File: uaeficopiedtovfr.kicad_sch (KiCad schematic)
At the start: 36 parts, among them J1 DTF13-12PB, J1 USB_B_Mini, J1 USB_C_Receptacle_USB2.0, J17 Conn_01x06, J4 DTF13-12PB, J5 Conn_01x05_Male, M1 Module-power_12and5V-0.2, M3 Module-knock-0.2, M3 Module-vr-discrete-0.4, M4 Module-vr-max9924-0.1, M5 Module-wbo-0.5, M6 Module:mega-mcu100/0.2, M7 Module-wbo-0.5, P1 Pad, P2 Pad, P3 Pad, P4 Pad, U4 JDY-33

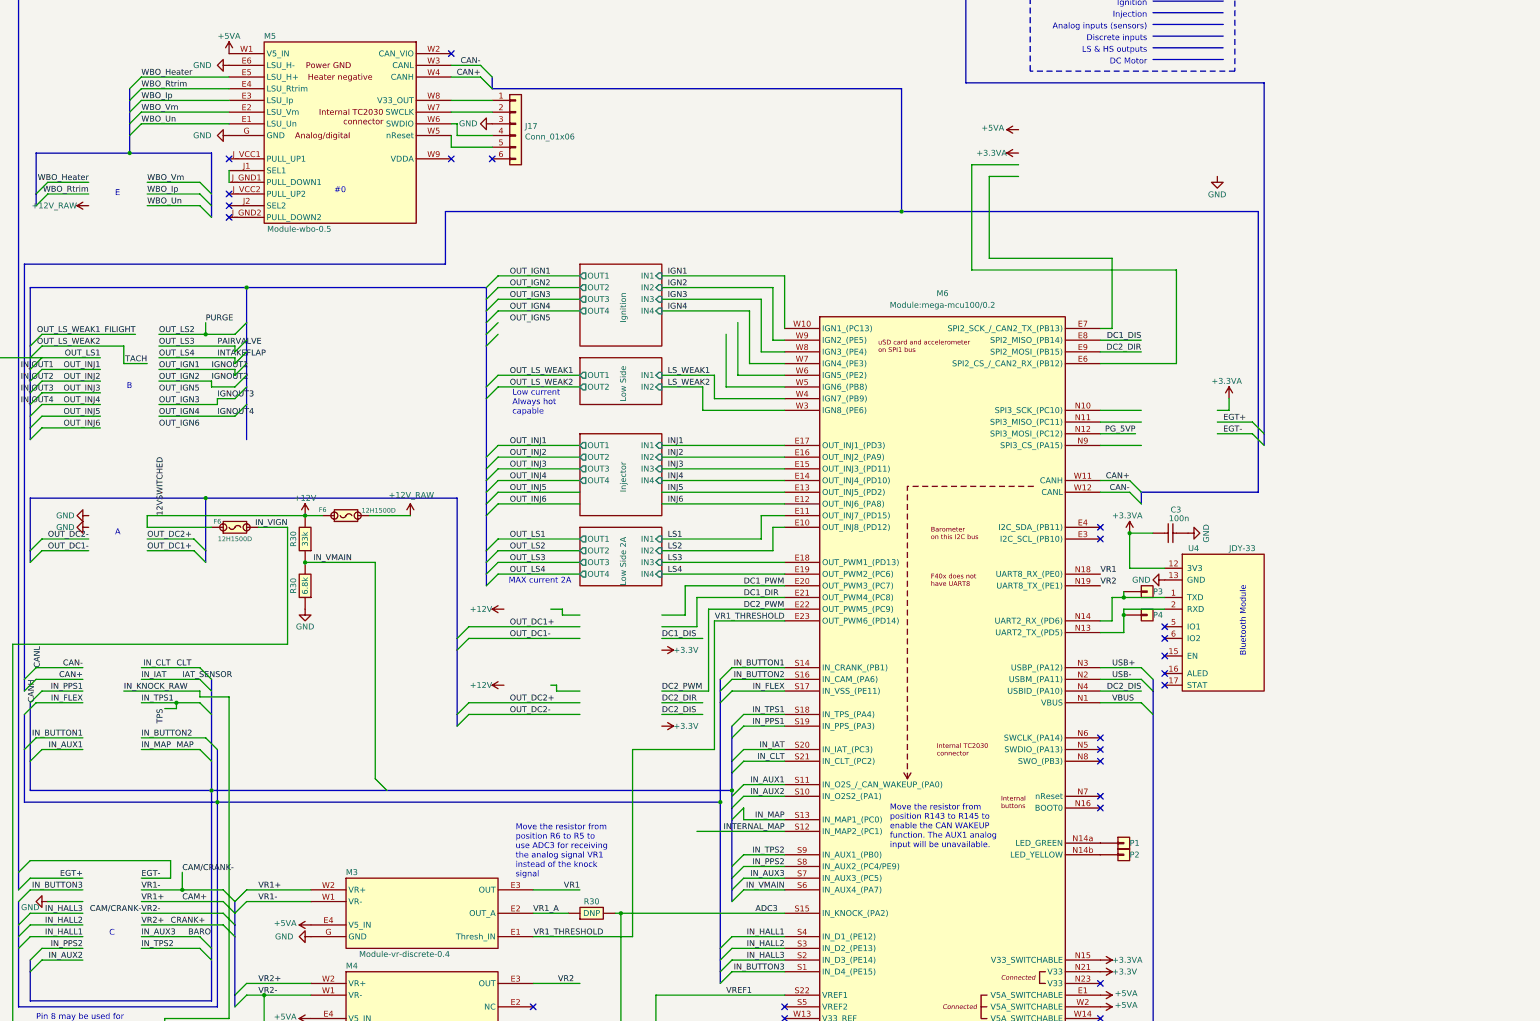
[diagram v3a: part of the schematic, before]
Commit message: Added SD card support, cleaned up ignition traces
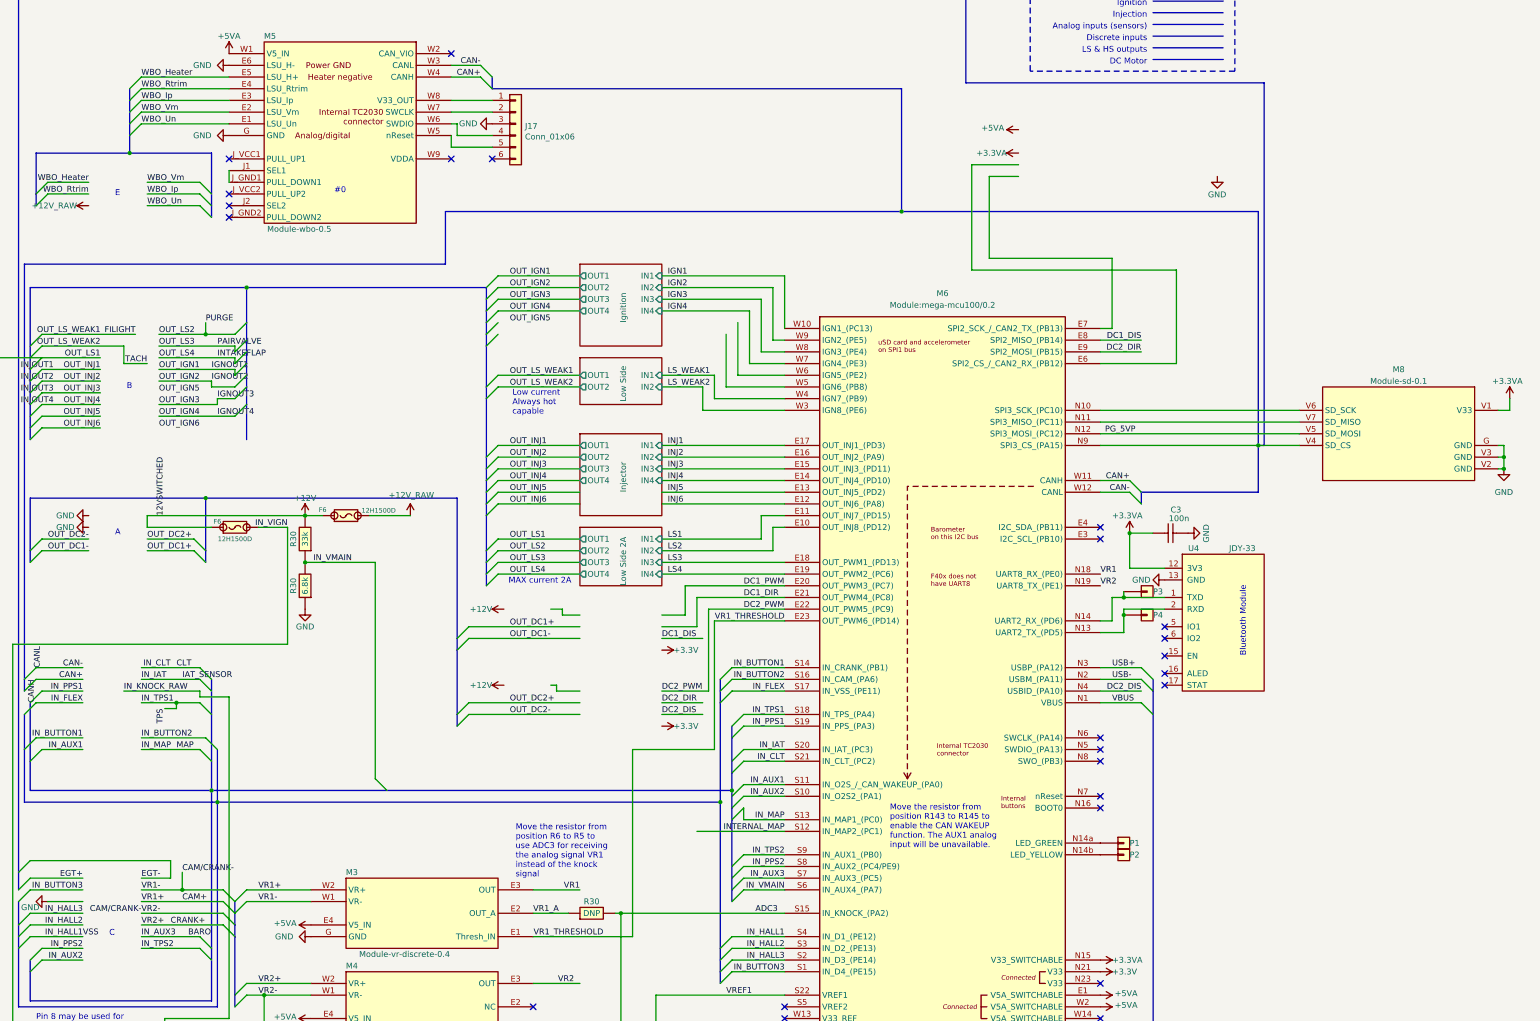
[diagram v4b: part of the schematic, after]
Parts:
- added M8: Module-sd-0.1, hellen-one-sd-0.1:sd, symbol hellen-one-sd:Module-sd-0.1
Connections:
- net VSS is gone; now on net IN_HALL1: U1.B17
- net +3.3VA: now also M8.V1 (V33)
- net GND: now also M8.G (GND), M8.V2 (GND), M8.V3 (GND)
- net PG_5VP: now also M8.V5 (SD_MOSI)
- net at M6.N10 (SPI3_SCK_(PC10)): now also M8.V6 (SD_SCK)
- net at M6.N11 (SPI3_MISO_(PC11)): now also M8.V7 (SD_MISO)
- net at M6.N9 (SPI3_CS_(PA15)): now also M8.V4 (SD_CS)
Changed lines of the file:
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@@
   (junction (at 259.08 210.82) (diameter 0) (color 0 0 0 0)
   )
+  (junction (at 375.92 133.35) (diameter 0) (color 0 0 0 0)
+  )
   (junction (at 347.98 152.4) (diameter 0) (color 0 0 0 0)
   )
@@
   (junction (at 334.01 344.17) (diameter 0) (color 0 0 0 0)
   )
+  (junction (at 429.26 135.89) (diameter 0) (color 0 0 0 0)
+  )
   (junction (at 20.32 72.39) (diameter 0) (color 0 0 0 0)
   )
   (junction (at 346.71 166.37) (diameter 0) (color 0 0 0 0)
   )
+  (junction (at 429.26 138.43) (diameter 0) (color 0 0 0 0)
+  )
   (junction (at 156.21 99.06) (diameter 0) (color 0 0 0 0)
   )
@@
     (stroke (width 0) (type default))
   )
-  (bus_entry (at 374.65 130.81) (size 2.54 2.54)
-    (stroke (width 0) (type default))
-  )
   (bus_entry (at 347.98 140.97) (size 2.54 2.54)
     (stroke (width 0) (type default))
@@
     (stroke (width 0) (type default))
   )
-  (bus_entry (at 374.65 128.27) (size 2.54 2.54)
-    (stroke (width 0) (type default))
-  )
   (bus_entry (at 111.76 242.57) (size -2.54 2.54)
     (stroke (width 0) (type default))
@@
     (stroke (width 0) (type default))
   )
+  (wire (pts (xy 429.26 138.43) (xy 429.26 135.89))
+    (stroke (width 0) (type default))
+  )
   (bus (pts (xy 208.28 135.89) (xy 208.28 138.43))
     (stroke (width 0) (type default) (color 255 153 0 1))
@@
     (stroke (width 0) (type default))
   )
+  (bus (pts (xy 375.92 133.35) (xy 375.92 82.55))
+    (stroke (width 0) (type default))
+  )
   (wire (pts (xy 153.67 120.65) (xy 148.59 120.65))
     (stroke (width 0) (type default))
   )
-  (wire (pts (xy 367.03 125.73) (xy 369.57 125.73))
+  (wire (pts (xy 427.99 125.73) (xy 430.53 125.73))
     (stroke (width 0) (type default))
   )
@@
     (stroke (width 0) (type default))
   )
-  (wire (pts (xy 367.03 128.27) (xy 374.65 128.27))
-    (stroke (width 0) (type default))
-  )
   (wire (pts (xy 344.17 107.95) (xy 344.17 92.71))
     (stroke (width 0) (type default))
@@
     (stroke (width 0) (type default))
   )
-  (bus (pts (xy 377.19 54.61) (xy 377.19 130.81))
+  (bus (pts (xy 377.19 54.61) (xy 377.19 133.35))
     (stroke (width 0) (type default))
   )
@@
     (stroke (width 0) (type default) (color 194 194 0 1))
   )
-  (bus (pts (xy 377.19 130.81) (xy 377.19 133.35))
-    (stroke (width 0) (type default))
-  )
   (wire (pts (xy 138.43 190.5) (xy 140.97 190.5))
     (stroke (width 0) (type default))
@@
     (stroke (width 0) (type default))
   )
-  (wire (pts (xy 369.57 125.73) (xy 369.57 123.19))
+  (wire (pts (xy 430.53 125.73) (xy 430.53 123.19))
     (stroke (width 0) (type default))
   )
-  (wire (pts (xy 341.63 125.73) (xy 350.52 125.73))
+  (wire (pts (xy 341.63 125.73) (xy 384.81 125.73))
     (stroke (width 0) (type default))
   )
@@
     (stroke (width 0) (type default))
   )
+  (wire (pts (xy 429.26 133.35) (xy 427.99 133.35))
+    (stroke (width 0) (type default))
+  )
   (wire (pts (xy 147.32 106.68) (xy 147.32 109.22))
     (stroke (width 0) (type default))
   )
+  (wire (pts (xy 375.92 133.35) (xy 384.81 133.35))
+    (stroke (width 0) (type default))
+  )
   (wire (pts (xy 265.43 104.14) (xy 265.43 115.57))
     (stroke (width 0) (type default))
@@
     (stroke (width 0) (type default))
   )
+  (wire (pts (xy 427.99 135.89) (xy 429.26 135.89))
+    (stroke (width 0) (type default))
+  )
   (wire (pts (xy 358.14 95.25) (xy 313.69 95.25))
     (stroke (width 0) (type default))
@@
     (stroke (width 0) (type default))
   )
+  (bus (pts (xy 375.92 133.35) (xy 377.19 133.35))
+    (stroke (width 0) (type default))
+  )
   (wire (pts (xy 260.35 109.22) (xy 260.35 120.65))
     (stroke (width 0) (type default))
@@
     (stroke (width 0) (type default))
   )
+  (wire (pts (xy 429.26 135.89) (xy 429.26 133.35))
+    (stroke (width 0) (type default))
+  )
   (bus (pts (xy 191.77 -19.05) (xy 191.77 -16.51))
     (stroke (width 0) (type default))
@@
     (stroke (width 0) (type default))
   )
-  (wire (pts (xy 341.63 128.27) (xy 350.52 128.27))
+  (wire (pts (xy 341.63 128.27) (xy 384.81 128.27))
     (stroke (width 0) (type default))
   )
@@
     (stroke (width 0) (type default))
   )
-  (bus (pts (xy 375.92 143.51) (xy 375.92 82.55))
+  (bus (pts (xy 375.92 143.51) (xy 375.92 133.35))
     (stroke (width 0) (type default))
   )
@@
     (stroke (width 0) (type default))
   )
-  (wire (pts (xy 341.63 133.35) (xy 350.52 133.35))
+  (wire (pts (xy 341.63 133.35) (xy 375.92 133.35))
     (stroke (width 0) (type default))
   )
@@
     (stroke (width 0) (type default) (color 194 194 0 1))
   )
+  (wire (pts (xy 427.99 138.43) (xy 429.26 138.43))
+    (stroke (width 0) (type default))
+  )
   (wire (pts (xy 246.38 186.69) (xy 256.54 186.69))
     (stroke (width 0) (type default))
@@
     (stroke (width 0) (type solid))
   )
-  (wire (pts (xy 349.25 130.81) (xy 341.63 130.81))
+  (wire (pts (xy 384.81 130.81) (xy 341.63 130.81))
     (stroke (width 0) (type default))
   )
@@
     (stroke (width 0) (type default) (color 0 194 194 1))
   )
-  (wire (pts (xy 367.03 130.81) (xy 374.65 130.81))
-    (stroke (width 0) (type default))
-  )
   (bus (pts (xy 350.52 146.05) (xy 350.52 143.51))
     (stroke (width 0) (type default))
@@
     (effects (font (size 1.27 1.27)) (justify right bottom))
   )
-  (label "EGT+" (at 368.3 128.27 0) (fields_autoplaced)
-    (effects (font (size 1.27 1.27)) (justify left bottom))
-  )
   (label "INJOUT1" (at 22.86 107.95 180) (fields_autoplaced)
     (effects (font (size 1.27 1.27)) (justify right bottom))
@@
     (effects (font (size 1.27 1.27)) (justify right bottom))
   )
+  (label "VSS" (at 120.65 240.03 0) (fields_autoplaced)
+    (effects (font (size 1.27 1.27)) (justify left bottom))
+  )
   (label "OUT_INJ4" (at 213.36 140.97 0) (fields_autoplaced)
     (effects (font (size 1.27 1.27)) (justify left bottom))
@@
     (effects (font (size 1.27 1.27)) (justify left bottom))
   )
-  (label "EGT-" (at 368.3 130.81 0) (fields_autoplaced)
-    (effects (font (size 1.27 1.27)) (justify left bottom))
-  )
   (label "IN_HALL3" (at 273.05 245.11 180) (fields_autoplaced)
     (effects (font (size 1.27 1.27)) (justify right bottom))
@@
     )
   )
+  (symbol (lib_id "power:GND") (at 429.26 138.43 0) (unit 1)
+    (in_bom yes) (on_board yes) (dnp no) (fields_autoplaced)
+    (property "Reference" "#PWR09" (at 429.26 144.78 0)
+      (effects (font (size 1.27 1.27)) hide)
+    )
+    (property "Value" "GND" (at 429.26 143.51 0)
+      (effects (font (size 1.27 1.27)))
+    )
+    (property "Footprint" "" (at 429.26 138.43 0)
+      (effects (font (size 1.27 1.27)) hide)
+    )
+    (property "Datasheet" "" (at 429.26 138.43 0)
+      (effects (font (size 1.27 1.27)) hide)
+    )
+    (pin "1")
+    (instances
+      (project "uaeficopiedtovfr"
+        (path "/90b72e19-92bc-40db-bd4d-f17fb5de93ea"
+          (reference "#PWR09") (unit 1)
+        )
+      )
+    )
+  )
   (symbol (lib_id "power:GND") (at 367.03 74.93 0) (mirror y) (unit 1)
     (in_bom yes) (on_board yes) (dnp no)
@@
     )
   )
+  (symbol (lib_id "hellen-one-sd:Module-sd-0.1") (at 389.89 120.65 0) (unit 1)
+    (in_bom yes) (on_board yes) (dnp no) (fields_autoplaced)
+    (property "Reference" "M8" (at 406.4 116.84 0)
+      (effects (font (size 1.27 1.27)))
+    )
+    (property "Value" "Module-sd-0.1" (at 406.4 119.38 0)
+      (effects (font (size 1.27 1.27)))
+    )
+    (property "Footprint" "hellen-one-sd-0.1:sd" (at 389.89 120.65 0)
+      (effects (font (size 1.27 1.27)) hide)
+    )
+    (property "Datasheet" "" (at 389.89 120.65 0)
+      (effects (font (size 1.27 1.27)) hide)
+    )
+    (pin "G")
+    (pin "V1")
+    (pin "V2")
+    (pin "V3")
+    (pin "V4")
+    (pin "V5")
+    (pin "V6")
+    (pin "V7")
+    (instances
+      (project "uaeficopiedtovfr"
+        (path "/90b72e19-92bc-40db-bd4d-f17fb5de93ea"
+          (reference "M8") (unit 1)
+        )
+      )
+    )
+  )
   (symbol (lib_id "customparts:VFR_PCB") (at 39.37 104.14 90) (unit 1)
     (in_bom yes) (on_board yes) (dnp no) (fields_autoplaced)
@@
     )
   )
-  (symbol (lib_id "power:+3.3VA") (at 369.57 123.19 0) (unit 1)
+  (symbol (lib_id "power:+3.3VA") (at 430.53 123.19 0) (unit 1)
     (in_bom yes) (on_board yes) (dnp no)
-    (property "Reference" "#PWR075" (at 369.57 127 0)
+    (property "Reference" "#PWR075" (at 430.53 127 0)
       (effects (font (size 1.27 1.27)) hide)
     )
-    (property "Value" "+3.3VA" (at 365.76 119.38 0)
+    (property "Value" "+3.3VA" (at 426.72 119.38 0)
       (effects (font (size 1.27 1.27)) (justify left))
     )
-    (property "Footprint" "" (at 369.57 123.19 0)
+    (property "Footprint" "" (at 430.53 123.19 0)
       (effects (font (size 1.27 1.27)) hide)
     )
-    (property "Datasheet" "" (at 369.57 123.19 0)
+    (property "Datasheet" "" (at 430.53 123.19 0)
       (effects (font (size 1.27 1.27)) hide)
     )

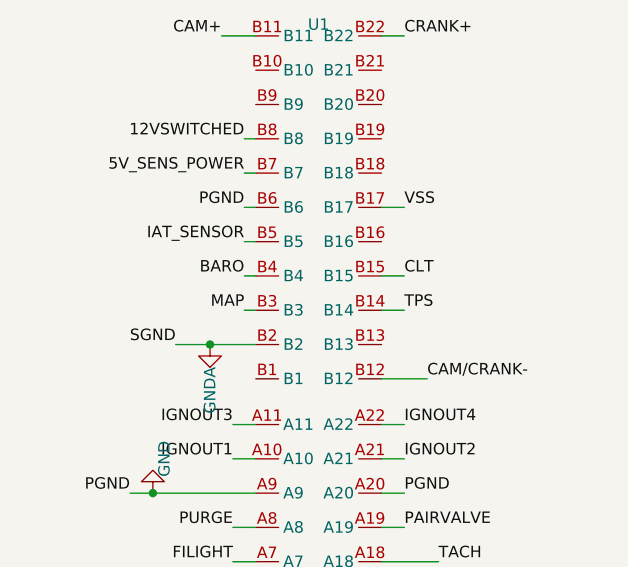
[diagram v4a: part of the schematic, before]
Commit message: Fixed error on connector pinout
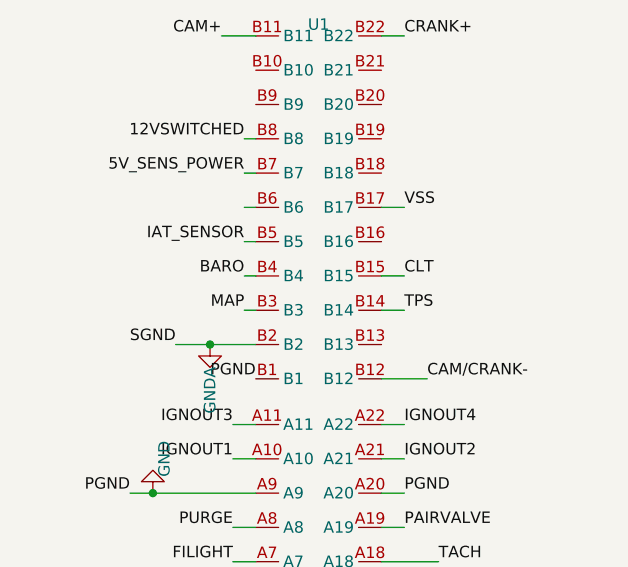
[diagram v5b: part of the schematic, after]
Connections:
- net GND: now also U1.B1; no longer U1.B6
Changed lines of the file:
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@@
+    (effects (font (size 1.27 1.27)) (justify right bottom))
+  )
+  (label "PGND" (at 25.4 76.2 180) (fields_autoplaced)
     (effects (font (size 1.27 1.27)) (justify right bottom))
   )
@@
     (effects (font (size 1.27 1.27)) (justify right bottom))
   )
-  (label "PGND" (at 24.13 57.15 180) (fields_autoplaced)
-    (effects (font (size 1.27 1.27)) (justify right bottom))
-  )
